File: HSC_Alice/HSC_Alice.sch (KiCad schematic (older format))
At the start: 13 parts

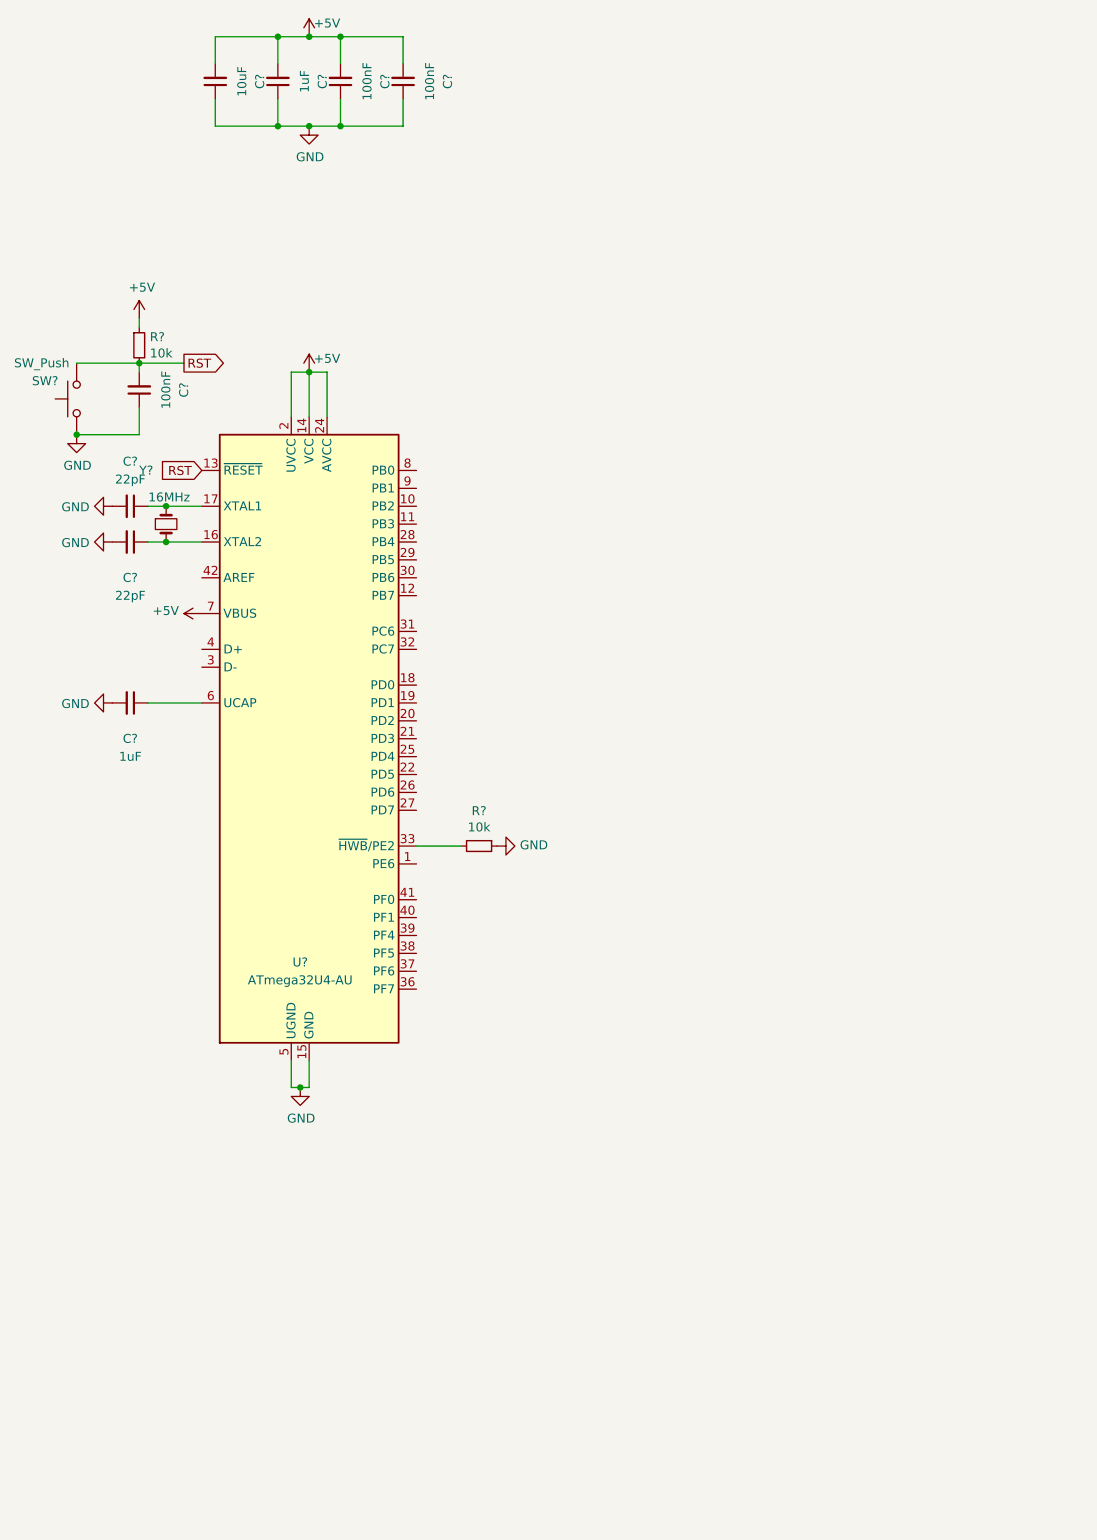
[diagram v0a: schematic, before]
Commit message: Removed faulty Acheron and Shark Library
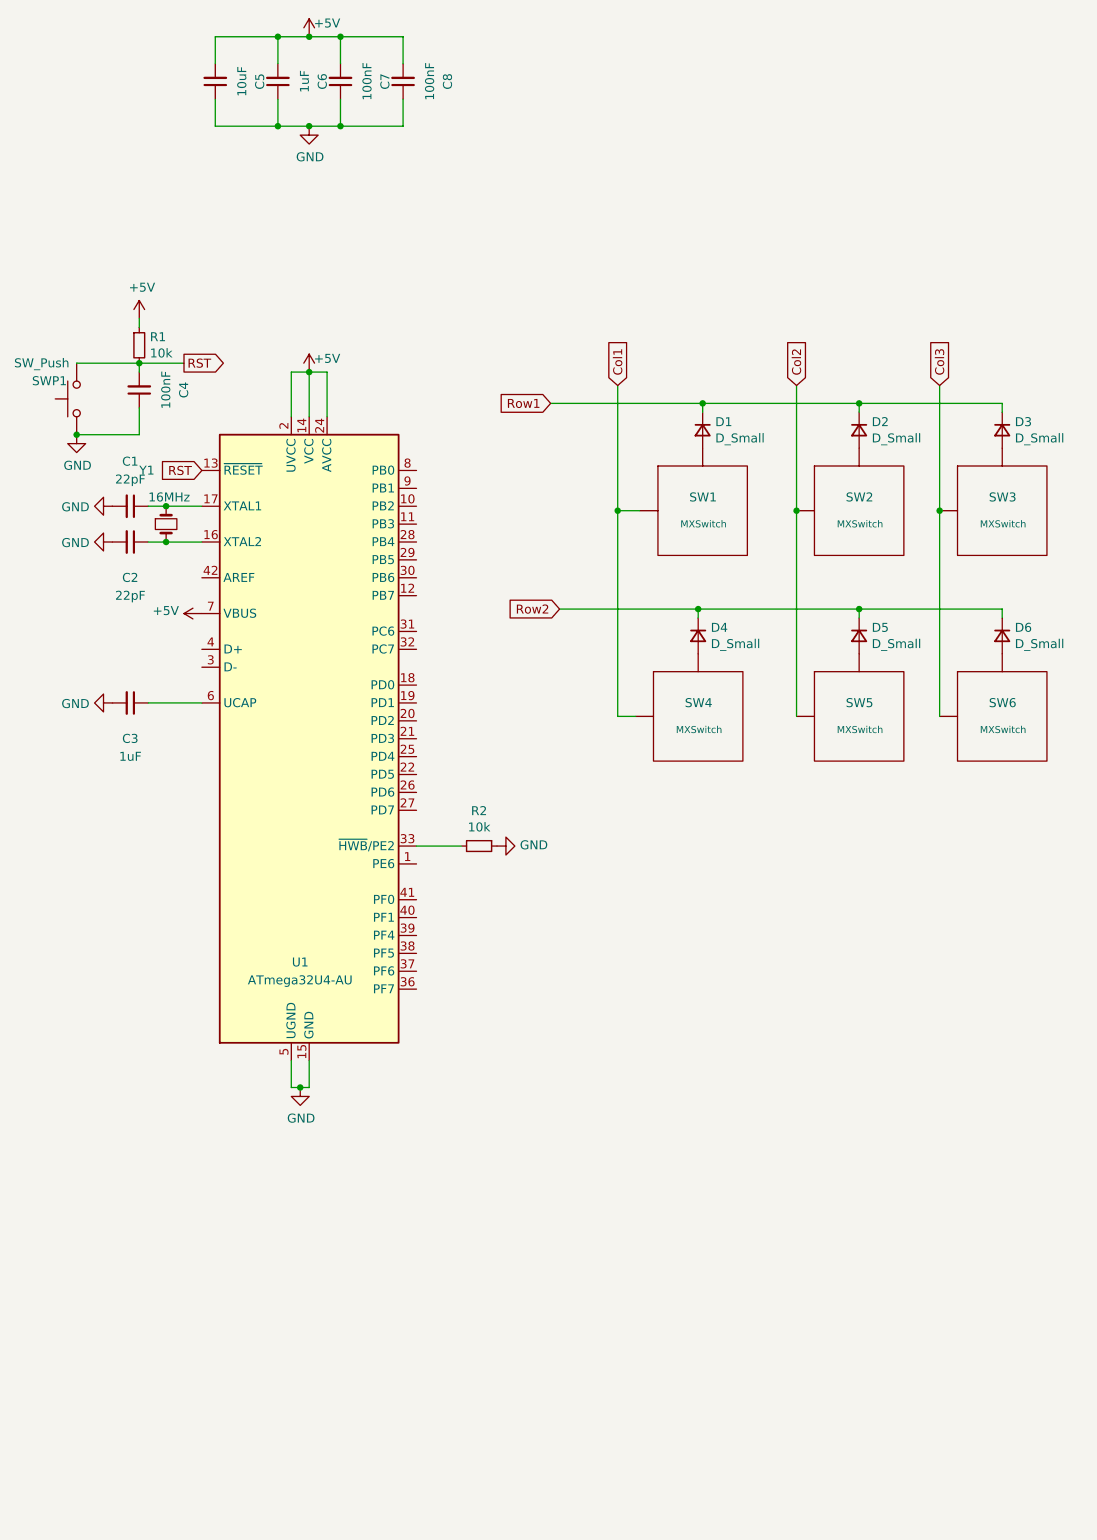
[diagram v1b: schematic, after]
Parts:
- added D1, D2, D3, D4, D5, D6: D_Small, Diode_SMD:D_SOD-123, symbol Device:D_Small
- added SW1, SW2, SW3, SW4, SW5, SW6: MXSwitch, Button_Switch_Keyboard:SW_Cherry_MX_1.00u_PCB, symbol shark50-cache:MXSwitch
- C1, C2, C3, C4, C5, C6, C7, C8: renamed from C?; footprint (none) -> Capacitor_SMD:C_0805_2012Metric_Pad1.18x1.45mm_HandSolder
- R1, R2: renamed from R?; footprint (none) -> Resistor_SMD:R_1206_3216Metric_Pad1.30x1.75mm_HandSolder
- Y1: renamed from Y?; footprint (none) -> Crystal:Crystal_SMD_5032-2Pin_5.0x3.2mm_HandSoldering
- gave numbers to parts that had none: 2
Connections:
- new net: D1.2 (A), SW1.2 (Row)
- new net: D2.2 (A), SW2.2 (Row)
- new net: D3.2 (A), SW3.2 (Row)
- new net: D4.2 (A), SW4.2 (Row)
- new net: D5.2 (A), SW5.2 (Row)
- new net: D6.2 (A), SW6.2 (Row)
- new net Col1: SW1.1 (Col), SW4.1 (Col)
- new net Col2: SW2.1 (Col), SW5.1 (Col)
- new net Col3: SW3.1 (Col), SW6.1 (Col)
- new net Row1: D1.1 (K), D2.1 (K), D3.1 (K)
- new net Row2: D4.1 (K), D5.1 (K), D6.1 (K)

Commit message: Add USB C connector
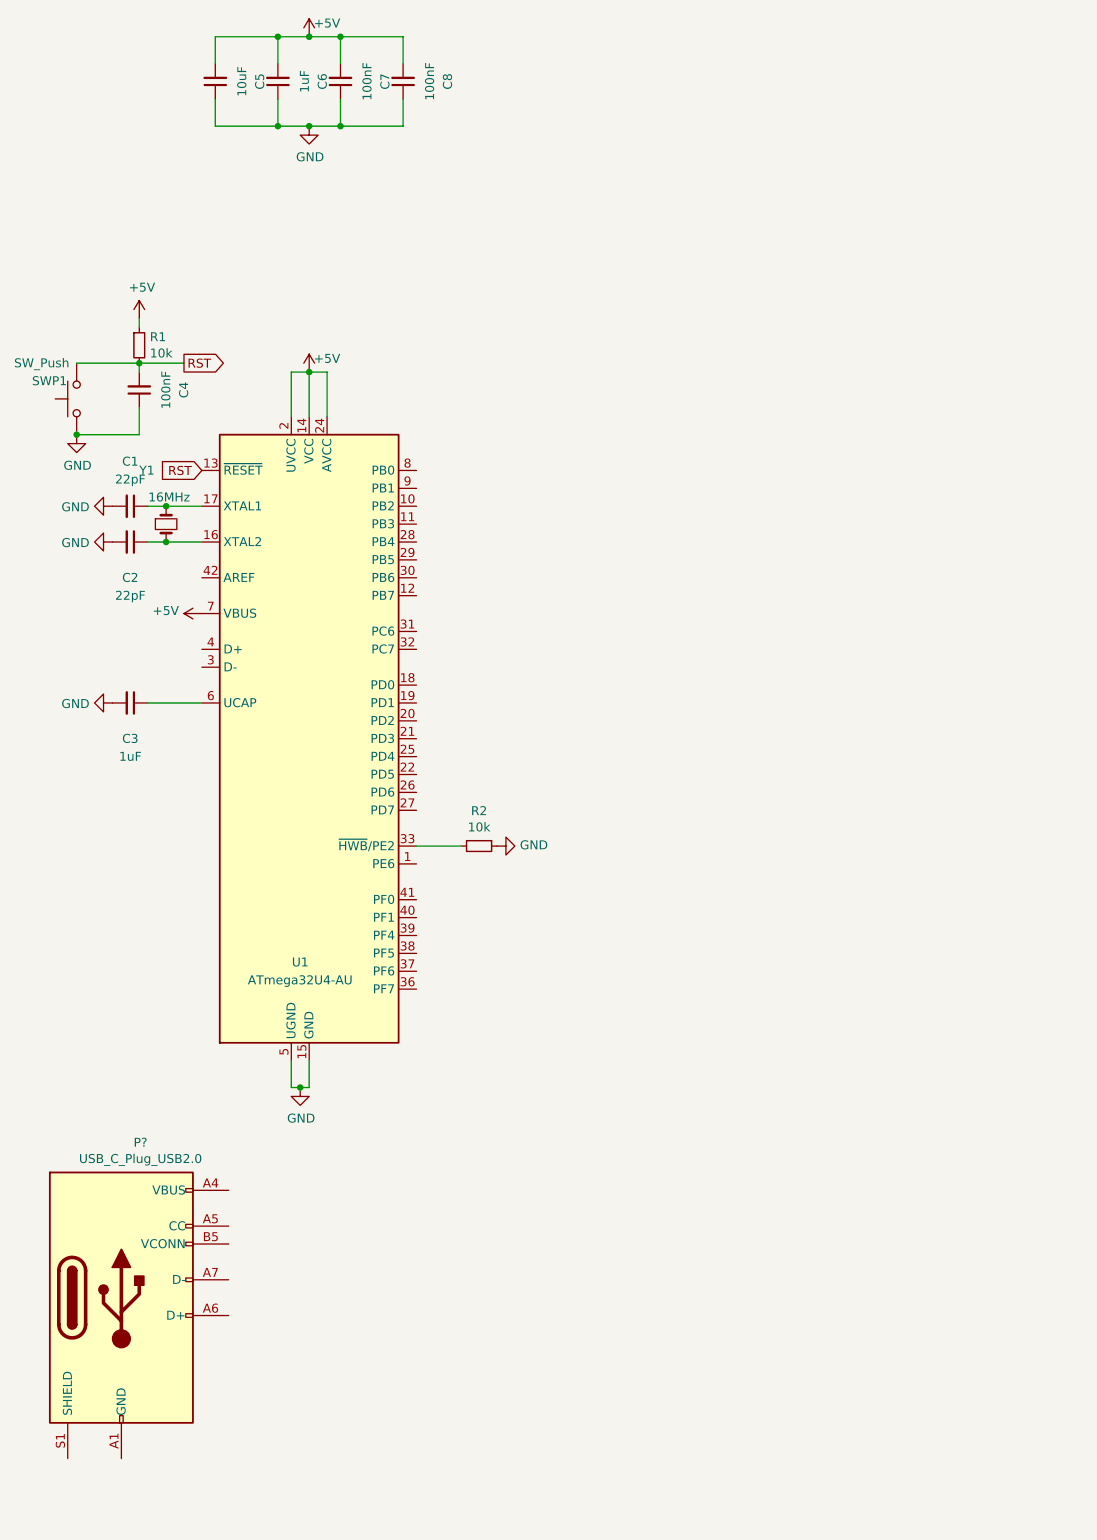
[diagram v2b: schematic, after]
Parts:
- removed D1, D2, D3, D4, D5, D6: D_Small, Diode_SMD:D_SOD-123, symbol Device:D_Small
- removed SW1, SW2, SW3, SW4, SW5, SW6: MXSwitch, Button_Switch_Keyboard:SW_Cherry_MX_1.00u_PCB, symbol shark50-cache:MXSwitch
- added P?: USB_C_Plug_USB2.0, symbol Connector:USB_C_Plug_USB2.0
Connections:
- new net: P?.A1 (GND), P?.A12 (GND), P?.B1 (GND), P?.B12 (GND)
- new net: P?.A4 (VBUS), P?.A9 (VBUS), P?.B4 (VBUS), P?.B9 (VBUS)
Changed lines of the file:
@@
 	2000 -825 2175 -825
 $Comp
-L shark50-cache:MXSwitch SW1
-U 1 1 60CB1F4A
-P 4200 1825
-F 0 "SW1" H 4125 1900 50  0000 L CNN
-F 1 "MXSwitch" H 4075 1750 39  0000 L CNN
-F 2 "Button_Switch_Keyboard:SW_Cherry_MX_1.00u_PCB" H 4200 1825 50  0001 C CNN
-F 3 "" H 4200 1825 50  0001 C CNN
-	1    4200 1825
+L Connector:USB_C_Plug_USB2.0 P?
+U 1 1 60D20649
+P 950 6225
+F 0 "P?" H 1057 7092 50  0000 C CNN
+F 1 "USB_C_Plug_USB2.0" H 1057 7001 50  0000 C CNN
+F 2 "" H 1100 6225 50  0001 C CNN
+F 3 "https://www.usb.org/sites/default/files/documents/usb_type-c.zip" H 1100 6225 50  0001 C CNN
+	1    950  6225
 	1    0    0    -1
 $EndComp
-$Comp
-L Device:D_Small D1
-U 1 1 60CB5654
-P 4200 1375
-F 0 "D1" V 4154 1445 50  0000 L CNN
-F 1 "D_Small" V 4245 1445 50  0000 L CNN
-F 2 "Diode_SMD:D_SOD-123" V 4200 1375 50  0001 C CNN
-F 3 "~" V 4200 1375 50  0001 C CNN
-	1    4200 1375
-	0    1    1    0
-$EndComp
-$Comp
-L shark50-cache:MXSwitch SW2
-U 1 1 60CB810B
-P 5075 1825
-F 0 "SW2" H 5000 1900 50  0000 L CNN
-F 1 "MXSwitch" H 4950 1750 39  0000 L CNN
-F 2 "Button_Switch_Keyboard:SW_Cherry_MX_1.00u_PCB" H 5075 1825 50  0001 C CNN
-F 3 "" H 5075 1825 50  0001 C CNN
-	1    5075 1825
-	1    0    0    -1
-$EndComp
-$Comp
-L Device:D_Small D2
-U 1 1 60CB8111
-P 5075 1375
-F 0 "D2" V 5029 1445 50  0000 L CNN
-F 1 "D_Small" V 5120 1445 50  0000 L CNN
-F 2 "Diode_SMD:D_SOD-123" V 5075 1375 50  0001 C CNN
-F 3 "~" V 5075 1375 50  0001 C CNN
-	1    5075 1375
-	0    1    1    0
-$EndComp
-$Comp
-L shark50-cache:MXSwitch SW3
-U 1 1 60CBC8B3
-P 5875 1825
-F 0 "SW3" H 5800 1900 50  0000 L CNN
-F 1 "MXSwitch" H 5750 1750 39  0000 L CNN
-F 2 "Button_Switch_Keyboard:SW_Cherry_MX_1.00u_PCB" H 5875 1825 50  0001 C CNN
-F 3 "" H 5875 1825 50  0001 C CNN
-	1    5875 1825
-	1    0    0    -1
-$EndComp
-$Comp
-L Device:D_Small D3
-U 1 1 60CBC8B9
-P 5875 1375
-F 0 "D3" V 5829 1445 50  0000 L CNN
-F 1 "D_Small" V 5920 1445 50  0000 L CNN
-F 2 "Diode_SMD:D_SOD-123" V 5875 1375 50  0001 C CNN
-F 3 "~" V 5875 1375 50  0001 C CNN
-	1    5875 1375
-	0    1    1    0
-$EndComp
-Text GLabel 3725 1125 1    50   Input ~ 0
-Col1
-Wire Wire Line
-	3725 1125 3725 1825
-Wire Wire Line
-	3725 1825 3850 1825
-Text GLabel 3350 1225 0    50   Input ~ 0
-Row1
-Wire Wire Line
-	3350 1225 4200 1225
-Wire Wire Line
-	4200 1225 4200 1275
-Wire Wire Line
-	5875 1225 5875 1275
-Wire Wire Line
-	4200 1225 5075 1225
-Connection ~ 4200 1225
-Wire Wire Line
-	5075 1225 5075 1275
-Connection ~ 5075 1225
-Wire Wire Line
-	5075 1225 5875 1225
-$Comp
-L shark50-cache:MXSwitch SW4
-U 1 1 60CD1397
-P 4175 2975
-F 0 "SW4" H 4100 3050 50  0000 L CNN
-F 1 "MXSwitch" H 4050 2900 39  0000 L CNN
-F 2 "Button_Switch_Keyboard:SW_Cherry_MX_1.00u_PCB" H 4175 2975 50  0001 C CNN
-F 3 "" H 4175 2975 50  0001 C CNN
-	1    4175 2975
-	1    0    0    -1
-$EndComp
-$Comp
-L Device:D_Small D4
-U 1 1 60CD139D
-P 4175 2525
-F 0 "D4" V 4129 2595 50  0000 L CNN
-F 1 "D_Small" V 4220 2595 50  0000 L CNN
-F 2 "Diode_SMD:D_SOD-123" V 4175 2525 50  0001 C CNN
-F 3 "~" V 4175 2525 50  0001 C CNN
-	1    4175 2525
-	0    1    1    0
-$EndComp
-$Comp
-L shark50-cache:MXSwitch SW5
-U 1 1 60CD13A3
-P 5075 2975
-F 0 "SW5" H 5000 3050 50  0000 L CNN
-F 1 "MXSwitch" H 4950 2900 39  0000 L CNN
-F 2 "Button_Switch_Keyboard:SW_Cherry_MX_1.00u_PCB" H 5075 2975 50  0001 C CNN
-F 3 "" H 5075 2975 50  0001 C CNN
-	1    5075 2975
-	1    0    0    -1
-$EndComp
-$Comp
-L Device:D_Small D5
-U 1 1 60CD13A9
-P 5075 2525
-F 0 "D5" V 5029 2595 50  0000 L CNN
-F 1 "D_Small" V 5120 2595 50  0000 L CNN
-F 2 "Diode_SMD:D_SOD-123" V 5075 2525 50  0001 C CNN
-F 3 "~" V 5075 2525 50  0001 C CNN
-	1    5075 2525
-	0    1    1    0
-$EndComp
-$Comp
-L Device:D_Small D6
-U 1 1 60CD13B5
-P 5875 2525
-F 0 "D6" V 5829 2595 50  0000 L CNN
-F 1 "D_Small" V 5920 2595 50  0000 L CNN
-F 2 "Diode_SMD:D_SOD-123" V 5875 2525 50  0001 C CNN
-F 3 "~" V 5875 2525 50  0001 C CNN
-	1    5875 2525
-	0    1    1    0
-$EndComp
-Wire Wire Line
-	4175 2375 4175 2425
-Wire Wire Line
-	3725 1825 3725 2975
-Wire Wire Line
-	3725 2975 3825 2975
-Connection ~ 3725 1825
-Text GLabel 3400 2375 0    50   Input ~ 0
-Row2
-Wire Wire Line
-	4175 2375 3400 2375
-Wire Wire Line
-	4725 1825 4725 2975
-Wire Wire Line
-	5525 2975 5525 1825
-Wire Wire Line
-	5525 1825 5525 1125
-Connection ~ 5525 1825
-Text GLabel 5525 1125 1    50   Input ~ 0
-Col3
-Wire Wire Line
-	5875 2425 5875 2375
-Wire Wire Line
-	5875 2375 5075 2375
-Connection ~ 4175 2375
-Wire Wire Line
-	5075 2425 5075 2375
-Connection ~ 5075 2375
-Wire Wire Line
-	5075 2375 4175 2375
-Wire Wire Line
-	4725 1825 4725 1125
-Connection ~ 4725 1825
-Text GLabel 4725 1125 1    50   Input ~ 0
-Col2
-$Comp
-L shark50-cache:MXSwitch SW6
-U 1 1 60CD13AF
-P 5875 2975
-F 0 "SW6" H 5800 3050 50  0000 L CNN
-F 1 "MXSwitch" H 5750 2900 39  0000 L CNN
-F 2 "Button_Switch_Keyboard:SW_Cherry_MX_1.00u_PCB" H 5875 2975 50  0001 C CNN
-F 3 "" H 5875 2975 50  0001 C CNN
-	1    5875 2975
-	1    0    0    -1
-$EndComp

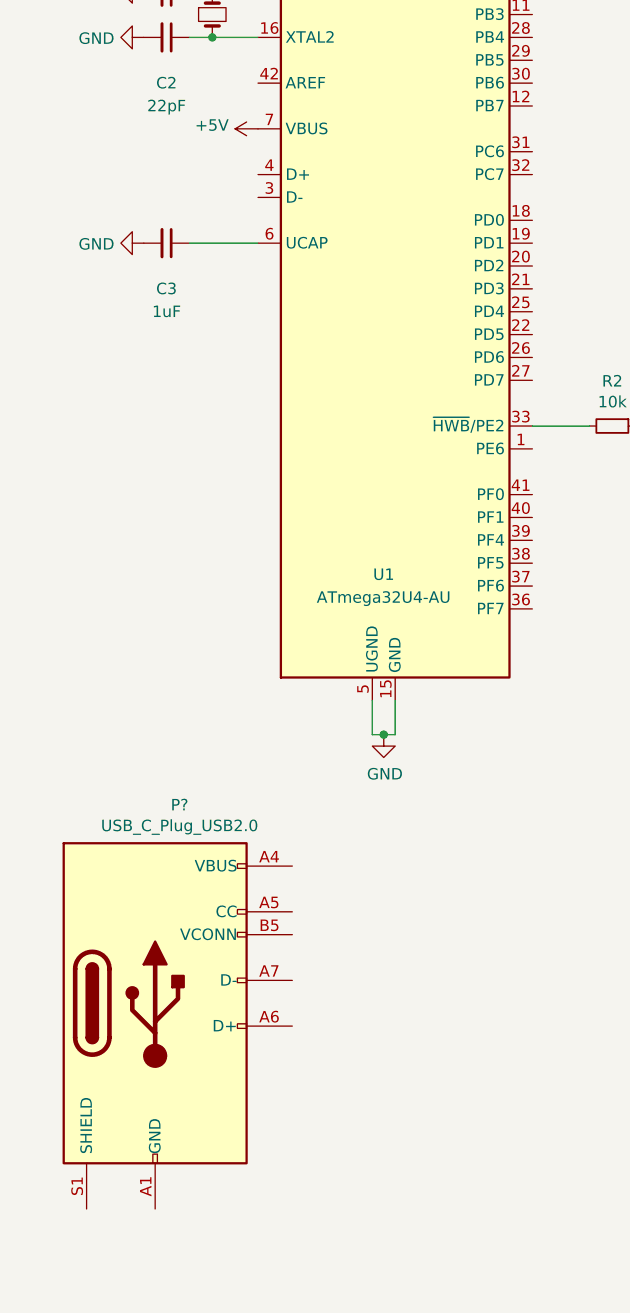
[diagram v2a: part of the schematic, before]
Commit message: Added Keebio components
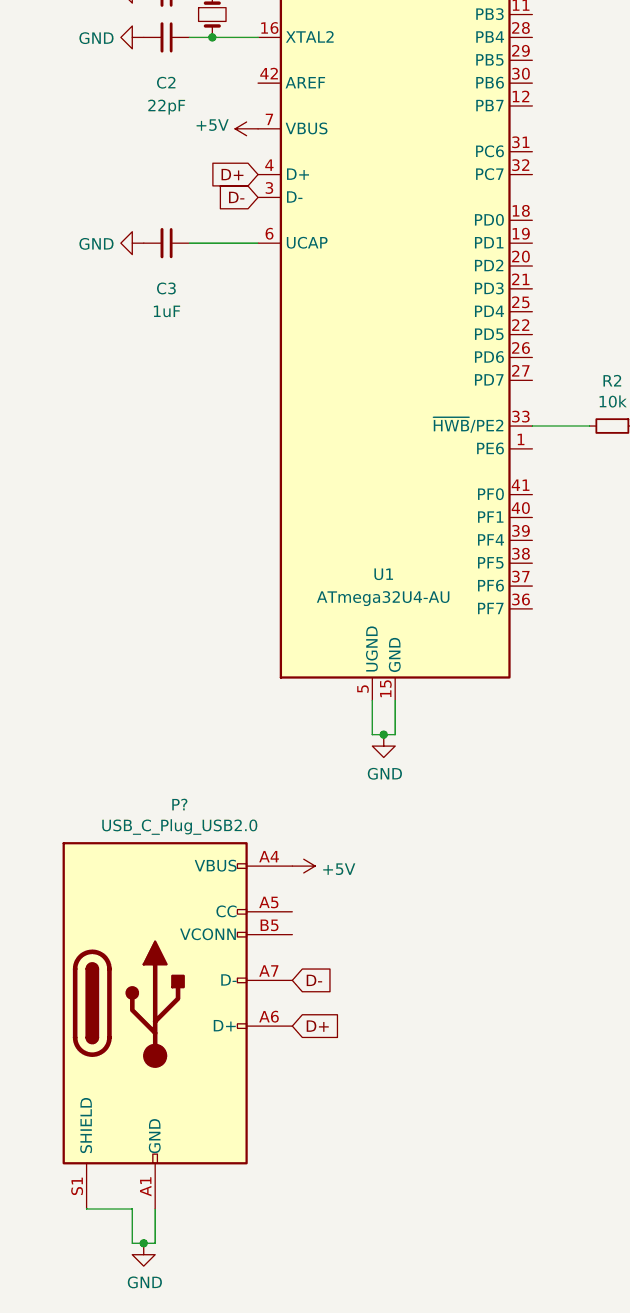
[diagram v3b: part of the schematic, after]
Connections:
- net +5V: now also P?.A4 (VBUS), P?.A9 (VBUS), P?.B4 (VBUS), P?.B9 (VBUS)
- net GND: now also P?.A1 (GND), P?.A12 (GND), P?.B1 (GND), P?.B12 (GND), P?.S1 (SHIELD)
- net D-: now reaches U1.3 (D-)
- net D-: now also P?.A7 (D-)
- net D+: now reaches U1.4 (D+)
- net D+: now also P?.A6 (D+)
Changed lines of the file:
@@
 	1    0    0    -1
 $EndComp
+$Comp
+L helix-cache:GND #PWR?
+U 1 1 60E67990
+P 900 7275
+F 0 "#PWR?" H 900 7025 50  0001 C CNN
+F 1 "GND" H 905 7102 50  0000 C CNN
+F 2 "" H 900 7275 50  0000 C CNN
+F 3 "" H 900 7275 50  0000 C CNN
+	1    900  7275
+	1    0    0    -1
+$EndComp
+Wire Wire Line
+	950  7125 950  7275
+Wire Wire Line
+	950  7275 900  7275
+Wire Wire Line
+	850  7125 850  7275
+Wire Wire Line
+	850  7275 900  7275
+Connection ~ 900  7275
+Wire Wire Line
+	850  7125 650  7125
+Text GLabel 1550 6125 2    50   Input ~ 0
+D-
+Text GLabel 1400 2700 0    50   Input ~ 0
+D-
+Text GLabel 1550 6325 2    50   Input ~ 0
+D+
+Text GLabel 1400 2600 0    50   Input ~ 0
+D+
+$Comp
+L power:+5V #PWR?
+U 1 1 60E6B79B
+P 1550 5625
+F 0 "#PWR?" H 1550 5475 50  0001 C CNN
+F 1 "+5V" V 1565 5753 50  0000 L CNN
+F 2 "" H 1550 5625 50  0001 C CNN
+F 3 "" H 1550 5625 50  0001 C CNN
+	1    1550 5625
+	0    1    1    0
+$EndComp
 $EndSCHEMATC
